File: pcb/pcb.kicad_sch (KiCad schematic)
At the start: 29 parts, among them J1 VDD, J10 SWDIO, J11 SWCLK, J2 GND, J3 LCD Data, J4 LCD RS, J5 LCD E, J6 3.3v, J7 ADC2, J8 GND, J9 USART1 TX, U1 TPS5430DDA, U2 STM32F446RETx

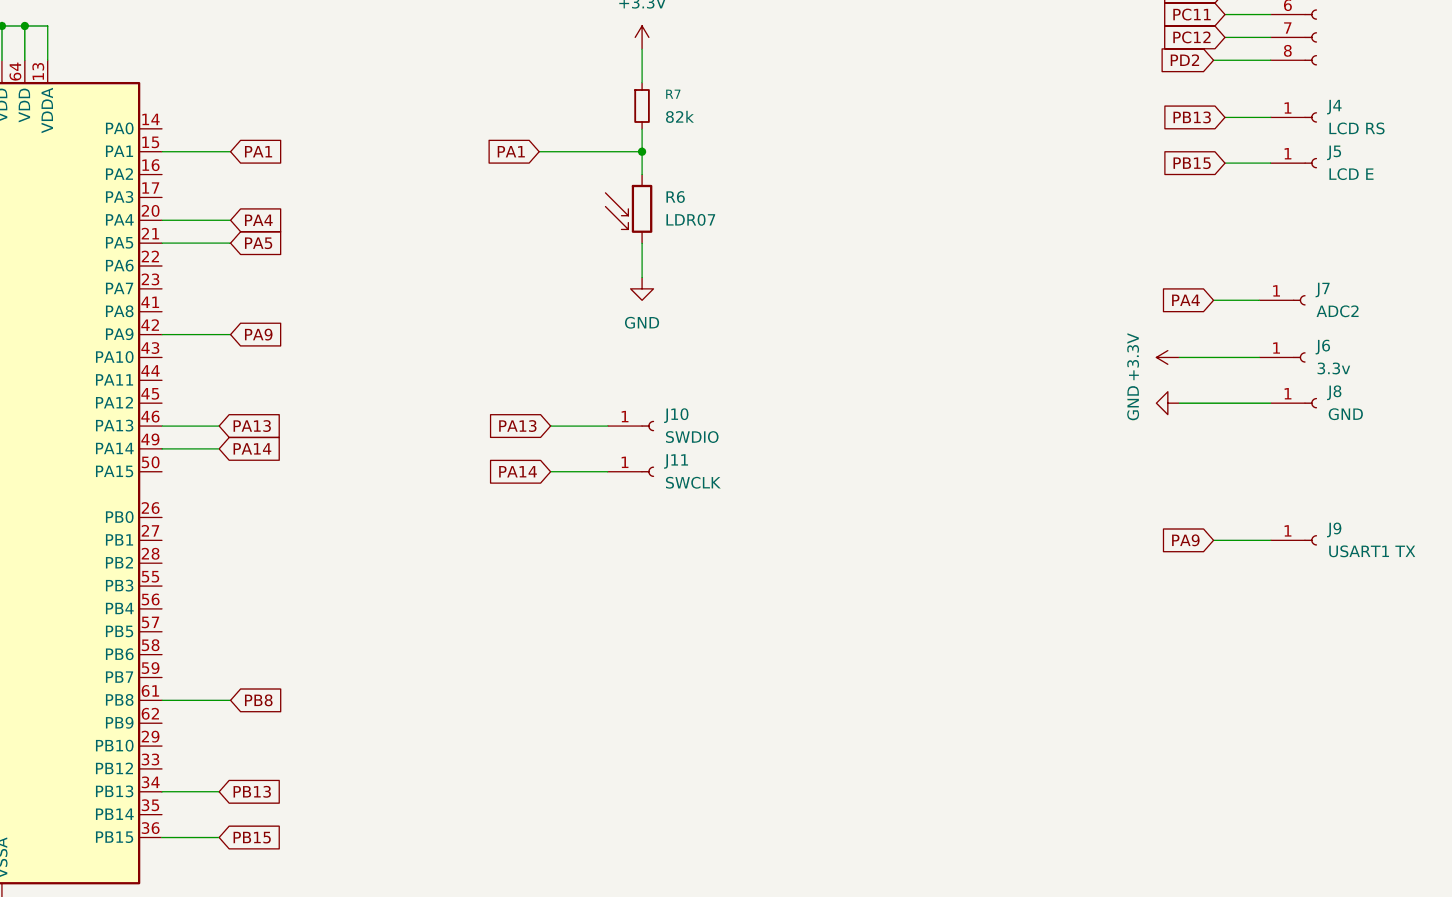
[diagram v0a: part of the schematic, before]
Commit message: add usart2 to schematic
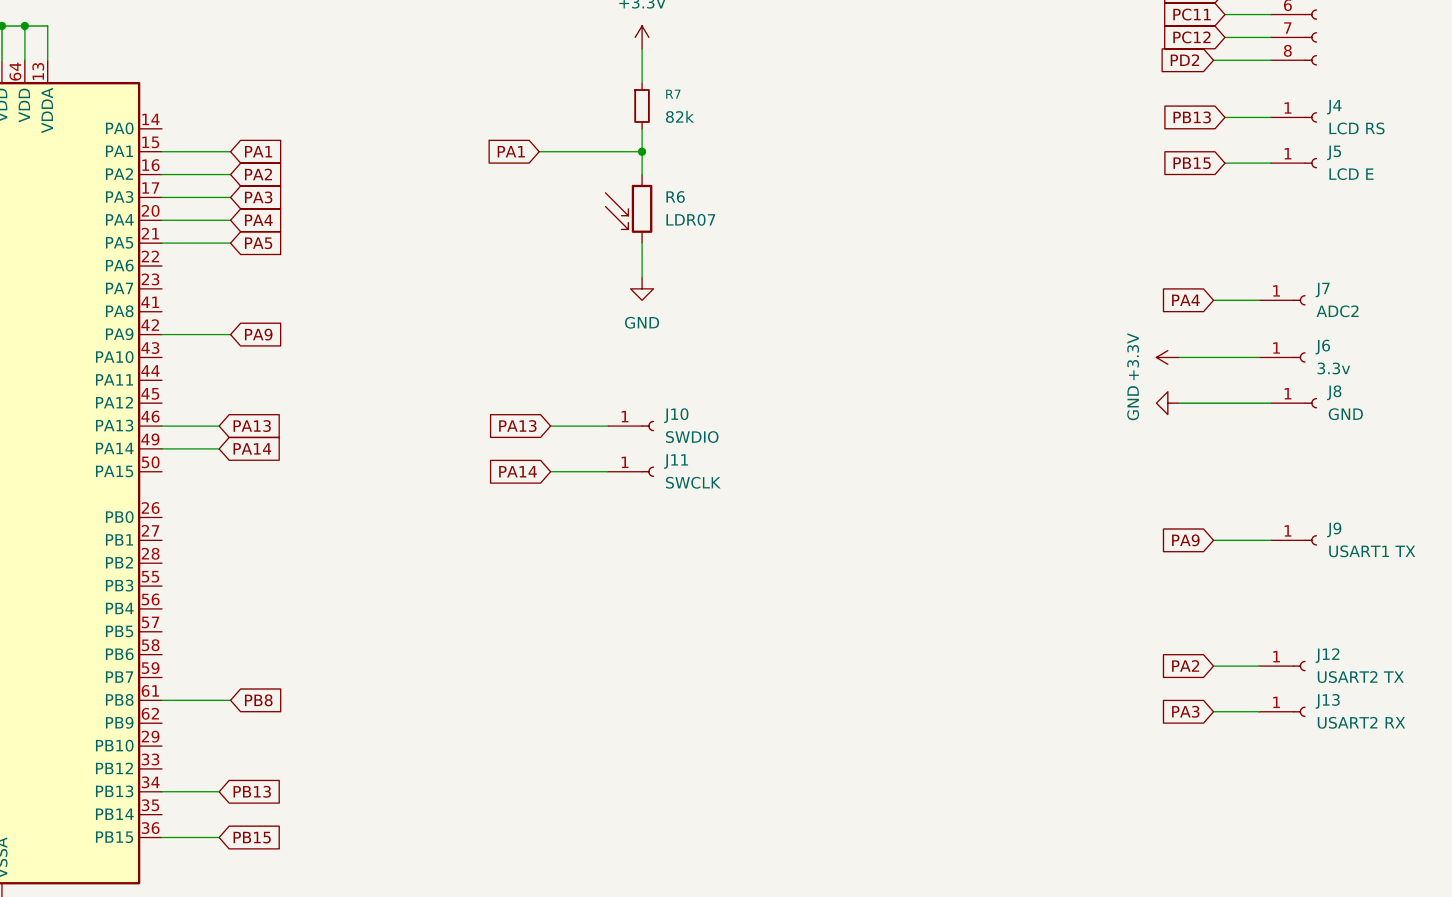
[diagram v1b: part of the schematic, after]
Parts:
- added J12: USART2 TX, symbol Connector:Conn_01x01_Socket
- added J13: USART2 RX, symbol Connector:Conn_01x01_Socket
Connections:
- net PA2: now reaches U2.16 (PA2)
- net PA2: now also J12.1 (Pin_1)
- net PA3: now reaches U2.17 (PA3)
- net PA3: now also J13.1 (Pin_1)

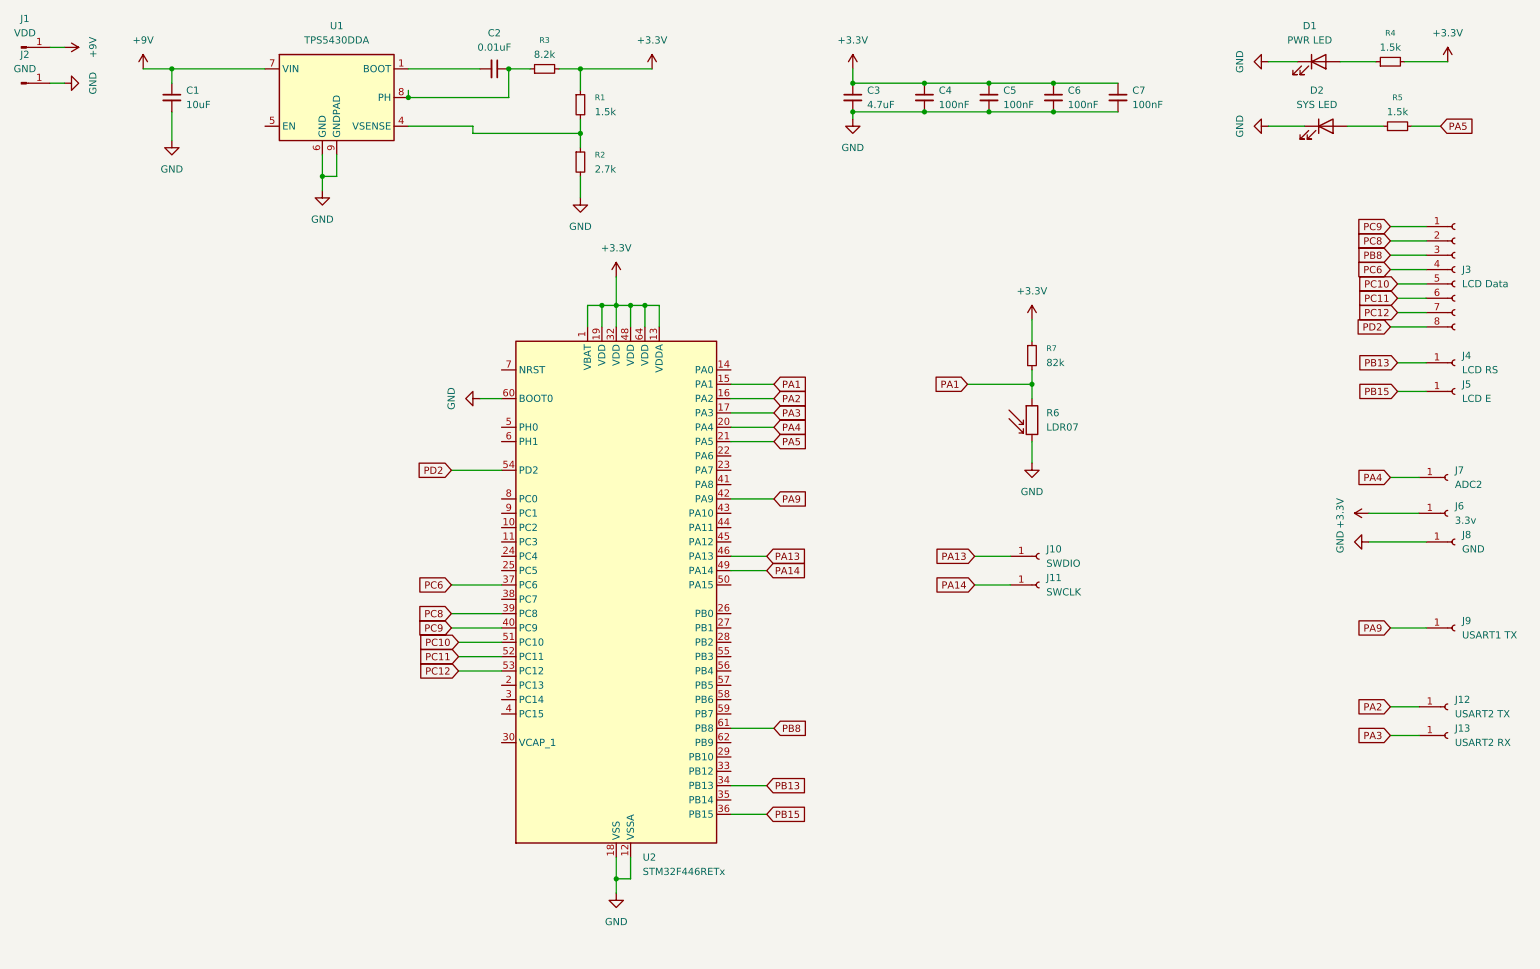
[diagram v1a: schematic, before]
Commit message: fix converter in schematic
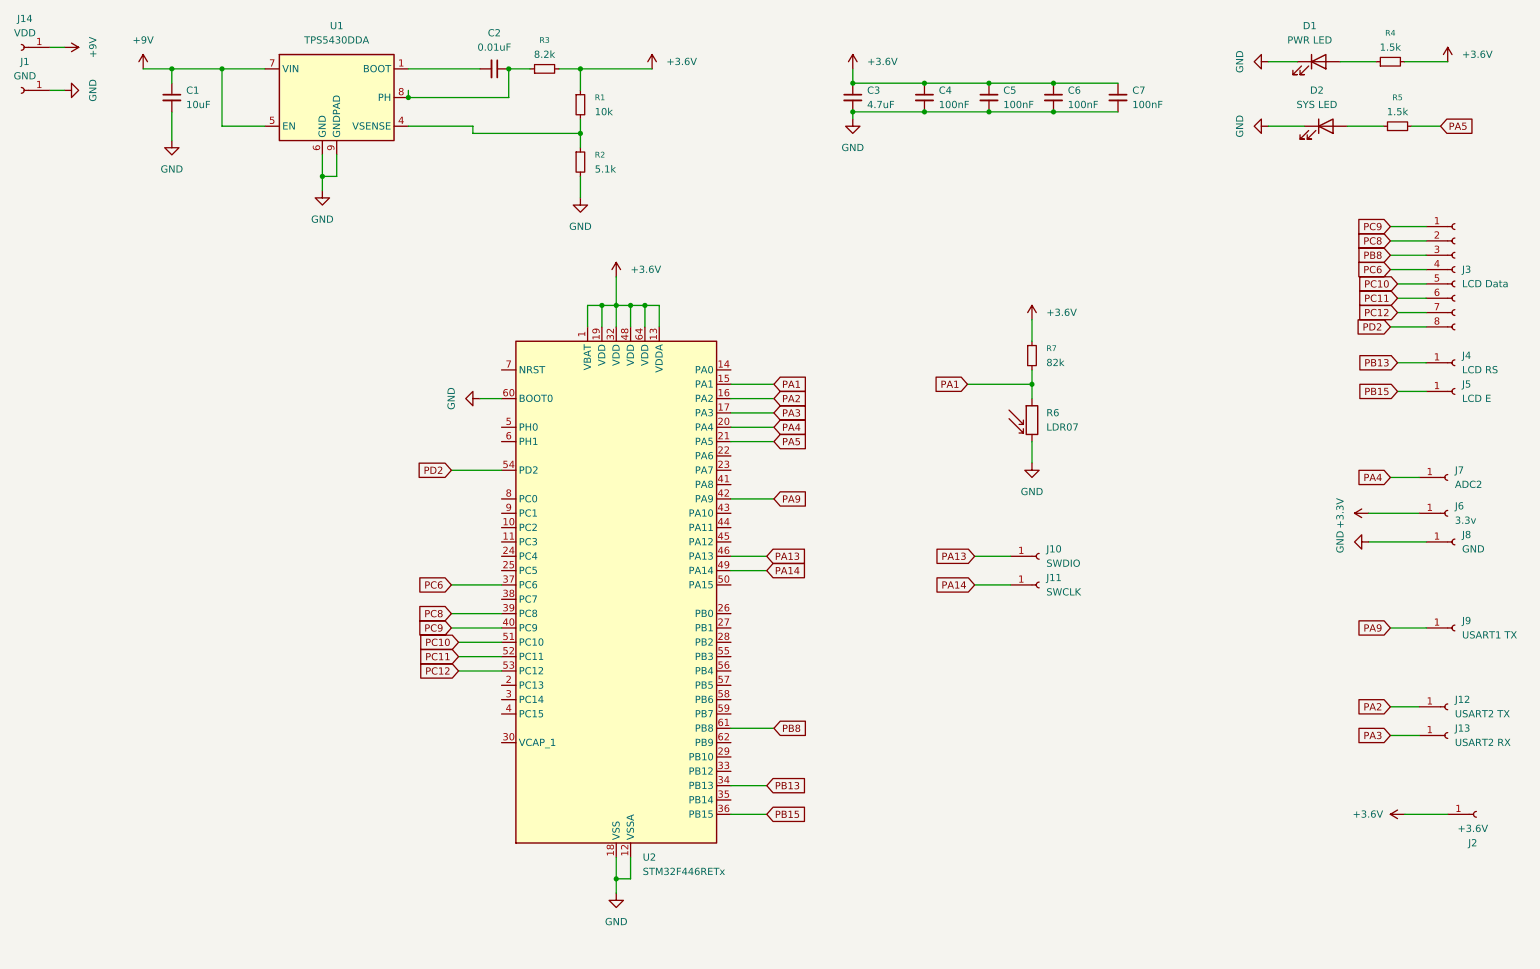
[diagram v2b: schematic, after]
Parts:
- removed J1: VDD, symbol Connector:Conn_01x01_Pin
- removed J2: GND, symbol Connector:Conn_01x01_Pin
- added J1: GND, symbol Connector:Conn_01x01_Socket
- added J14: VDD, symbol Connector:Conn_01x01_Socket
- added J2: +3.6V, symbol Connector:Conn_01x01_Socket
- R1: value 1.5k -> 10k
- R2: value 2.7k -> 5.1k
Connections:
- net +3.3V: no longer C3.1, C4.1, C5.1, C6.1, C7.1, R1.1, R3.2, R4.2, R7.1, U2.1 (VBAT), U2.13 (VDDA), U2.19 (VDD), U2.32 (VDD), U2.48 (VDD), U2.64 (VDD)
- net +9V: now also U1.5 (EN), J14.1 (Pin_1)
- net GND: now also J1.1 (Pin_1)
- new net +3.6V: C3.1, C4.1, C5.1, C6.1, C7.1, J2.1 (Pin_1), R1.1, R3.2, R4.2, R7.1, U2.1 (VBAT), U2.13 (VDDA), U2.19 (VDD), U2.32 (VDD), U2.48 (VDD), U2.64 (VDD)

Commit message: update schematic and readme
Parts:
- removed R3: 8.2k, symbol Device:R_Small
- removed U1: TPS5430DDA, Package_SO:TI_SO-PowerPAD-8_ThermalVias, symbol Regulator_Switching:TPS5430DDA
- added C10, C9: 100nF, symbol Device:C_Small
- added C8: 6.8pF, symbol Device:C_Small
- added L1: 2.2uH, symbol Device:L_Small
- added U1: TLV62569DBV, Package_TO_SOT_SMD:SOT-23-5, symbol Regulator_Switching:TLV62569DBV
- C1: value 10uF -> 4.7uF
- C2: value 0.01uF -> 10uF
- R1: value 10k -> 900k
- R2: value 5.1k -> 200k
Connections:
- net +3.6V is gone; now on net +3.3V: C3.1, C4.1, C5.1, C6.1, C7.1, J2.1 (Pin_1), R1.1, R4.2, R7.1, U2.1 (VBAT), U2.13 (VDDA), U2.19 (VDD), U2.32 (VDD), U2.48 (VDD), U2.64 (VDD)
- net +3.3V: now also C2.1, U2.30 (VCAP_1), C10.1, C8.1, C9.1, L1.2
- net GND: now also C2.2, C10.2, C9.2, U1.2 (GND)
- net at R1.2, R2.1: now also C8.2, U1.5 (FB)
- net +9V renamed +5V
- net +5V: now also U1.1 (EN), U1.4 (VIN)
- new net: L1.1, U1.3 (SW)
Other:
- moved on the sheet: C1, C3, C4, C5, C6, C7, J8, R1, R2
